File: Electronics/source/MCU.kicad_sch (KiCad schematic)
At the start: 52 parts, among them J1 Conn_01x05, J16 Conn_01x02, J2 Conn_01x03, J3 Conn_01x03, J4 Conn_01x05, J6 Conn_01x20, J7 Conn_01x20, SW10 SW_Push, SW11 SW_Push, SW12 SW_Push, SW13 SW_Push, SW14 SW_Coded, SW4 SW_Push, SW5 SW_SPDT, SW6 SW_SPDT, SW7 SW_SPDT, SW8 SW_Push, SW9 SW_Push, U1 STM32F030C8Tx, U4 FT231XS, U5 ADP122AUJZ-3.3-R7, Y1 ABL-8.000MHZ-B2

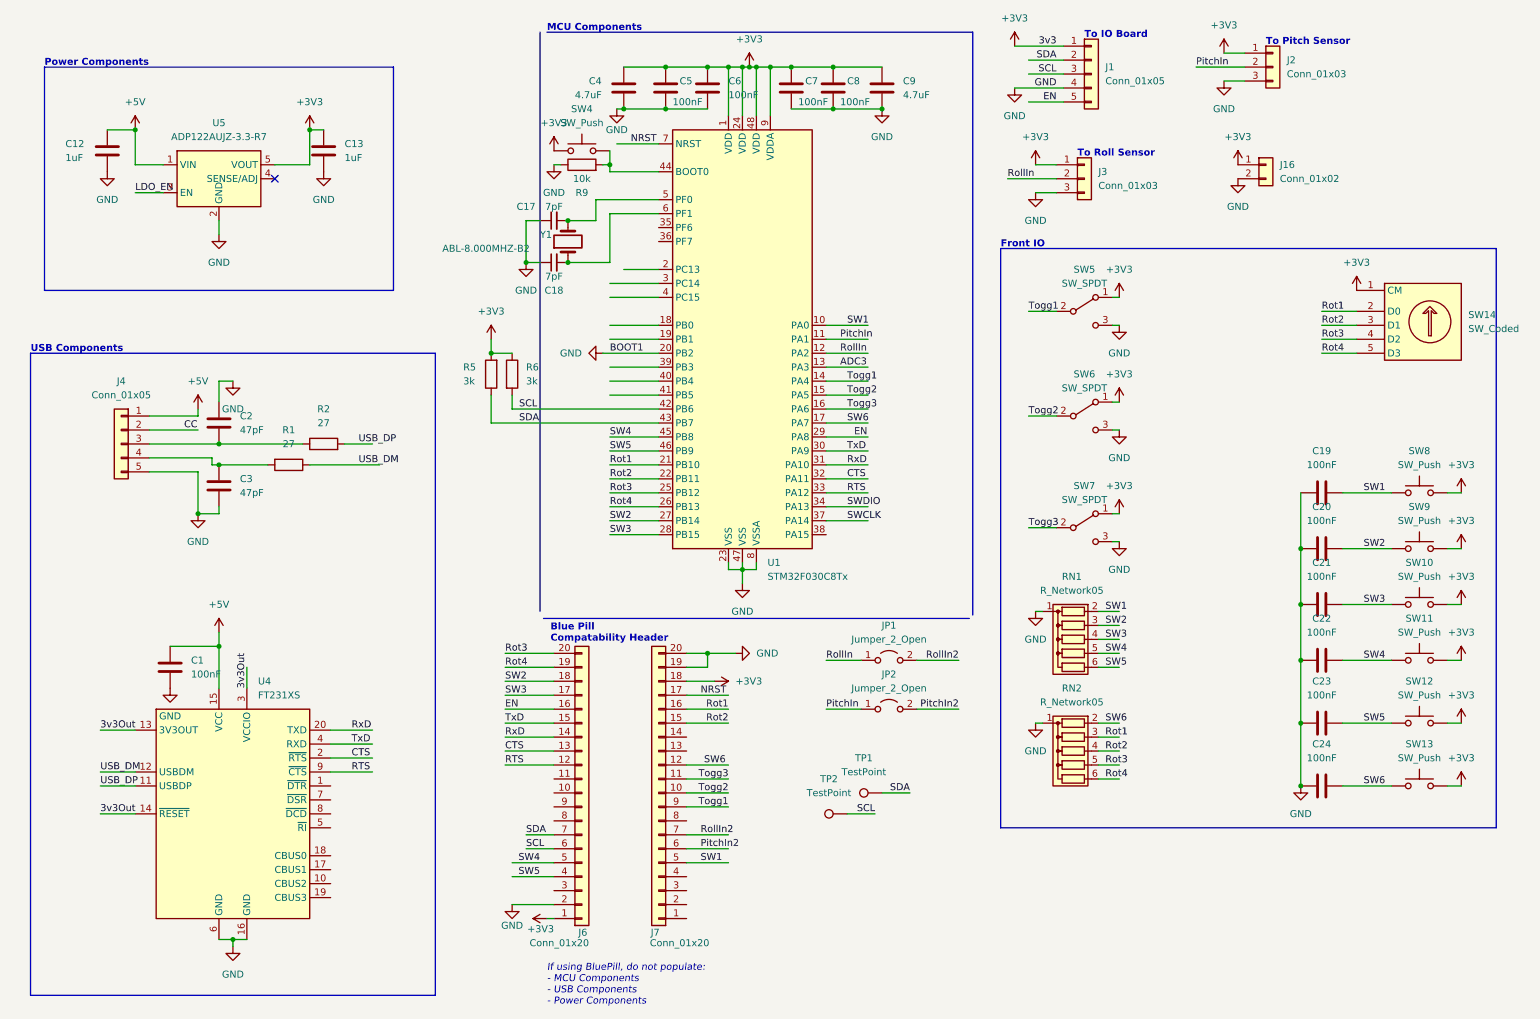
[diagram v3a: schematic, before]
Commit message: Changed MCU to STM32F072 variant with built-in USB and removed wrong FTDI chip
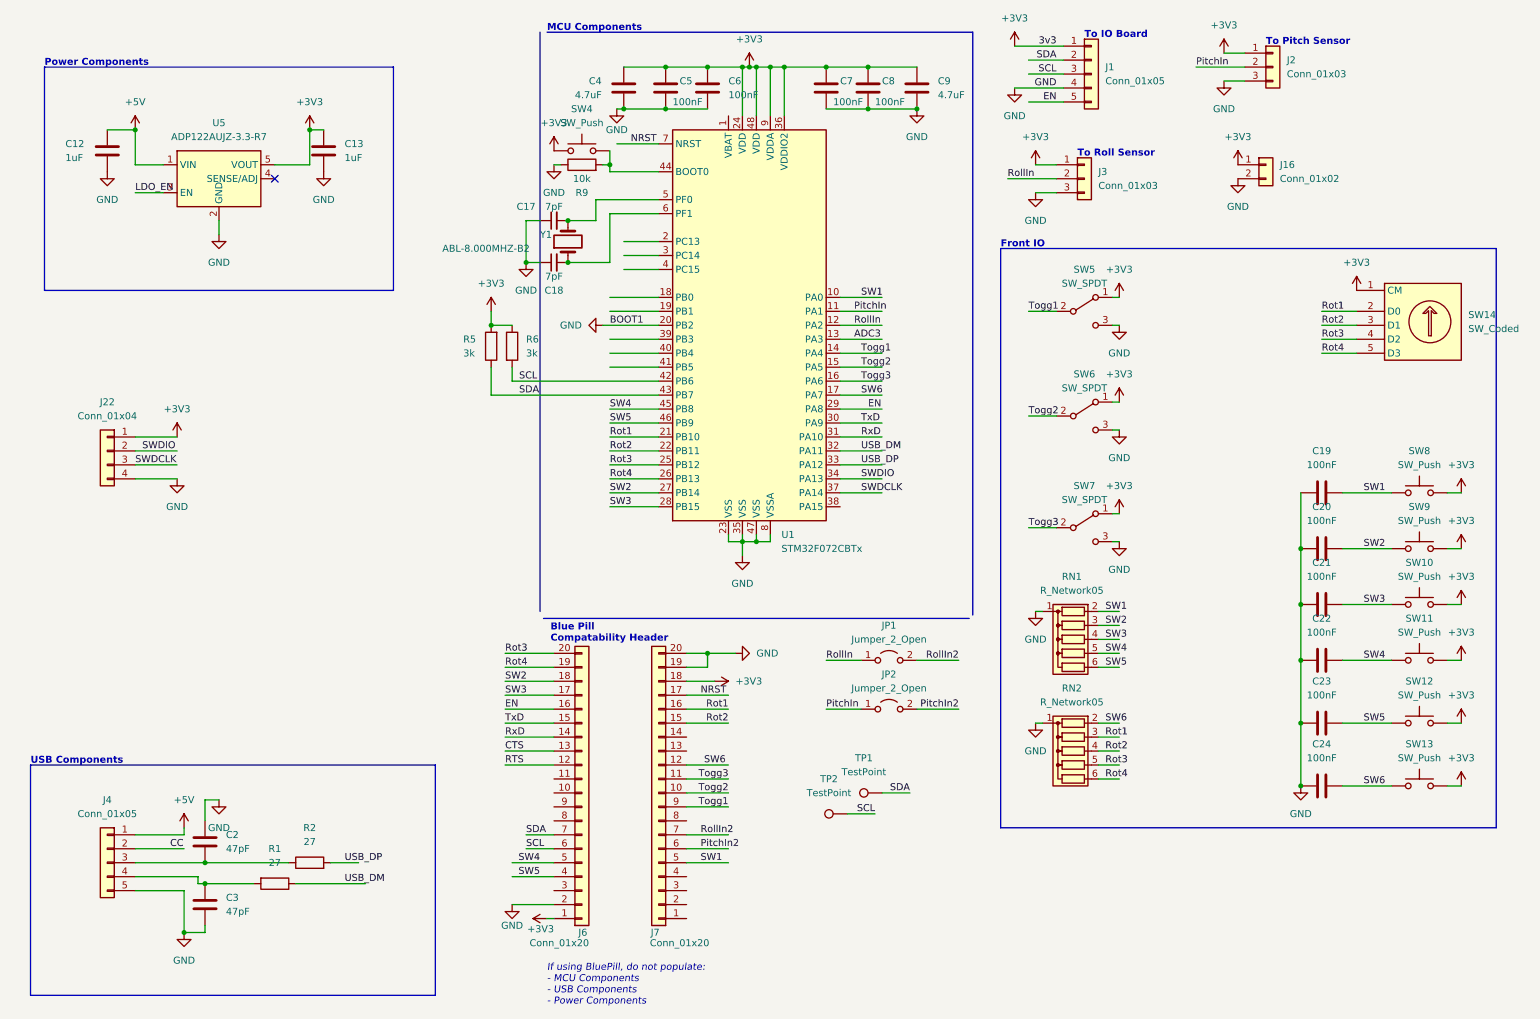
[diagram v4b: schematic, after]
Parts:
- removed C1: 100nF, Capacitor_SMD:C_0805_2012Metric, symbol Device:C
- removed U1: STM32F030C8Tx, Package_QFP:LQFP-48_7x7mm_P0.5mm, symbol MCU_ST_STM32F0:STM32F030C8Tx
- removed U4: FT231XS, Package_SO:SSOP-20_3.9x8.7mm_P0.635mm, symbol Interface_USB:FT231XS
- added J22: Conn_01x04, Connector_PinHeader_2.54mm:PinHeader_1x04_P2.54mm_Vertical, symbol Connector_Generic:Conn_01x04
- added U1: STM32F072CBTx, Package_QFP:LQFP-48_7x7mm_P0.5mm, symbol MCU_ST_STM32F0:STM32F072CBTx
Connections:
- net +3V3: now also J22.1 (Pin_1), U1.24 (VDD), U1.36 (VDDIO2), U1.48 (VDD), U1.9 (VDDA)
- net ADC3: now also U1.13 (PA3)
- net EN: now also U1.29 (PA8)
- net GND: now also J22.4 (Pin_4), U1.20 (PB2), U1.23 (VSS), U1.35 (VSS), U1.47 (VSS), U1.8 (VSSA)
- net NRST: now also U1.7 (NRST)
- net PitchIn: now also U1.11 (PA1)
- net RollIn: now also U1.12 (PA2)
- net Rot1: now also U1.21 (PB10)
- net Rot2: now also U1.22 (PB11)
- net Rot3: now also U1.25 (PB12)
- net Rot4: now also U1.26 (PB13)
- net RxD: now also U1.31 (PA10)
- net SCL: now also U1.42 (PB6)
- net SDA: now also U1.43 (PB7)
- net SW1: now also U1.10 (PA0)
- net SW2: now also U1.27 (PB14)
- net SW3: now also U1.28 (PB15)
- net SW4: now also U1.45 (PB8)
- net SW5: now also U1.46 (PB9)
- net SW6: now also U1.17 (PA7)
- net SWDIO: now also J22.2 (Pin_2), U1.34 (PA13)
- net Togg1: now also U1.14 (PA4)
- net Togg2: now also U1.15 (PA5)
- net Togg3: now also U1.16 (PA6)
- net TxD: now also U1.30 (PA9)
- net USB_DM: now also U1.32 (PA11)
- net USB_DP: now also U1.33 (PA12)
- net at R9.2, SW4.2: now also U1.44 (BOOT0)
- net at C17.2, Y1.2: now also U1.5 (PF0)
- net at C18.2, Y1.1: now also U1.6 (PF1)
- new net SWDCLK: J22.3 (Pin_3), U1.37 (PA14)
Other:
- moved on the sheet: C2, C3, C7, C8, C9, J4, R1, R2, R5, R6
